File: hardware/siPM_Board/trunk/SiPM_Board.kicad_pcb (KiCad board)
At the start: 2 copper layers, 25 parts, among them J1 Conn_02x34_Odd_Even, J2 Conn_02x34_Odd_Even, U1 LM94021, U2 S14161-6050HS-04, U3 S14161-6050HS-04, U4 S14161-6050HS-04, U5 S14161-6050HS-04

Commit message: Layout Needs Editing
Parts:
- C1, C10, C11, C12, C13, C14, C15, C16, C17, C18, C2, C3, C4, C5, C6, C7, C8, C9, J1, J2, U1: moved to B.Cu
- moved U5 60.6 mm to (156.0, 88.5)
- moved U2 60.0 mm to (130.5, 88.5)
- moved C17 44.6 mm to (138.1, 92.1), turned to 90 degrees
- moved C13 39.9 mm to (141.5, 92.1), turned to 90 degrees
- moved C16 36.3 mm to (138.1, 98.2), turned to 90 degrees
- moved J1 36.1 mm to (130.5, 101.5), turned to 270 degrees
- moved C9 35.3 mm to (144.8, 92.1), turned to 90 degrees
- moved U1 32.7 mm to (143.2, 117.7)
- moved C18 32.5 mm to (141.4, 83.5), turned to 90 degrees
- moved C12 31.7 mm to (141.5, 98.2), turned to 90 degrees
- moved C5 30.7 mm to (148.2, 92.1), turned to 90 degrees
- moved C1 28.2 mm to (144.8, 83.5), turned to 90 degrees
- moved C15 28.0 mm to (138.1, 104.2), turned to 90 degrees
- moved C8 27.1 mm to (144.8, 98.2), turned to 90 degrees
- moved U3 26.8 mm to (130.5, 114.0)
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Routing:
- added copper zone on SiPM_Bias_voltage, net /BIAS1
- added copper zone on GND, net GND
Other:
- board outline added: 50.7 x 50.7 mm
- copper layers 2 -> 4

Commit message: Modified Perliminary Layout
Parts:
- moved U4 25.5 mm to (155.9, 88.5)
- moved U5 25.5 mm to (156.0, 114.0)
- turned J2 to 270 degrees

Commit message: Schematic changes made
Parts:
- removed C11, C12, C13, C14, C15, C16, C17, C18: 100nF, Capacitor_SMD:C_1206_3216Metric_Pad1.33x1.80mm_HandSolder
- C1, C10, C2, C3, C4, C5, C6, C7, C8, C9: footprint Capacitor_SMD:C_1206_3216Metric_Pad1.33x1.80mm_HandSolder -> Capacitor_SMD:C_0603_1608Metric_Pad1.08x0.95mm_HandSolder
- U1: footprint TO_SOT_Packages_SMD:Texas_R-PDSO-G6 -> Arich_SiPM_Footprints:Texas_R-PDSO-G6
- moved C1 16.5 mm to (139.4, 99.2), turned to 270 degrees
- moved C9 14.8 mm to (141.1, 106.5), turned to 180 degrees
- moved C2 12.7 mm to (141.9, 99.2), turned to 270 degrees
- moved C6 11.3 mm to (147.3, 99.2), turned to 270 degrees
- moved C4 9.50 mm to (140.3, 103.4), turned to 270 degrees
- moved C5 7.98 mm to (144.4, 99.2), turned to 270 degrees
- moved C3 6.21 mm to (142.0, 103.4), turned to 270 degrees
- moved C10 5.40 mm to (145.3, 106.4), turned to 180 degrees
- moved C8 5.39 mm to (144.4, 103.5), turned to 270 degrees
- moved C7 2.21 mm to (146.9, 103.4), turned to 270 degrees
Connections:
- C10 pad 1: /BIAS2 -> /OUT
- C3 pad 1: /BIAS1 -> /BIAS2
- C4 pad 1: /BIAS1 -> /BIAS2
- C5 pad 1: /BIAS1 -> /BIAS3
- C6 pad 1: /BIAS1 -> /BIAS3
- C7 pad 1: /BIAS1 -> /BIAS4
- C7 pad 2: GND -> Net-(C7-Pad2)
- C8 pad 1: /BIAS1 -> /BIAS4
- C8 pad 2: GND -> Net-(C7-Pad2)
- C9 pad 1: /BIAS2 -> /VDD
- J1 pad 2: GND -> /BIAS1
- J1 pad 66: /OUT -> GND
- J1 pad 67: /BIAS1 -> /BIAS2
- J1 pad 68: /BIAS1 -> /OUT
- J2 pad 2: GND -> /BIAS3
- J2 pad 66: Net-(J2-Pad66) -> GND
- J2 pad 67: /BIAS2 -> /BIAS4
- J2 pad 68: /BIAS2 -> /BIAS4
- U3 pad B1: /BIAS1 -> /BIAS2
- U3 pad B3: /BIAS1 -> /BIAS2
- U3 pad B5: /BIAS1 -> /BIAS2
- U3 pad B7: /BIAS1 -> /BIAS2
- U3 pad D1: /BIAS1 -> /BIAS2
- U3 pad D3: /BIAS1 -> /BIAS2
- U3 pad D5: /BIAS1 -> /BIAS2
- U3 pad D7: /BIAS1 -> /BIAS2
- U3 pad F2: /BIAS1 -> /BIAS2
- U3 pad F4: /BIAS1 -> /BIAS2
- U3 pad F6: /BIAS1 -> /BIAS2
- U3 pad F8: /BIAS1 -> /BIAS2
- U3 pad H2: /BIAS1 -> /BIAS2
- U3 pad H4: /BIAS1 -> /BIAS2
- U3 pad H6: /BIAS1 -> /BIAS2
- U3 pad H8: /BIAS1 -> /BIAS2
- U4 pad B1: /BIAS2 -> /BIAS3
- U4 pad B3: /BIAS2 -> /BIAS3
- U4 pad B5: /BIAS2 -> /BIAS3
- U4 pad B7: /BIAS2 -> /BIAS3
- U4 pad D1: /BIAS2 -> /BIAS3
- U4 pad D3: /BIAS2 -> /BIAS3
- U4 pad D5: /BIAS2 -> /BIAS3
- U4 pad D7: /BIAS2 -> /BIAS3
- U4 pad F2: /BIAS2 -> /BIAS3
- U4 pad F4: /BIAS2 -> /BIAS3
- U4 pad F6: /BIAS2 -> /BIAS3
- U4 pad F8: /BIAS2 -> /BIAS3
- U4 pad H2: /BIAS2 -> /BIAS3
- U4 pad H4: /BIAS2 -> /BIAS3
- U4 pad H6: /BIAS2 -> /BIAS3
- U4 pad H8: /BIAS2 -> /BIAS3
- U5 pad B1: /BIAS2 -> /BIAS4
- U5 pad B3: /BIAS2 -> /BIAS4
- U5 pad B5: /BIAS2 -> /BIAS4
- U5 pad B7: /BIAS2 -> /BIAS4
- U5 pad D1: /BIAS2 -> /BIAS4
- U5 pad D3: /BIAS2 -> /BIAS4
- U5 pad D5: /BIAS2 -> /BIAS4
- U5 pad D7: /BIAS2 -> /BIAS4
- U5 pad F2: /BIAS2 -> /BIAS4
- U5 pad F4: /BIAS2 -> /BIAS4
- U5 pad F6: /BIAS2 -> /BIAS4
- U5 pad F8: /BIAS2 -> /BIAS4
- U5 pad H2: /BIAS2 -> /BIAS4
- U5 pad H4: /BIAS2 -> /BIAS4
- U5 pad H6: /BIAS2 -> /BIAS4
- U5 pad H8: /BIAS2 -> /BIAS4

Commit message: Tracing incomplete
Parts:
- moved U1 5.64 mm to (143.3, 112.0), turned to 180 degrees
- moved C10 2.56 mm to (143.2, 107.9), turned to 0 degrees
- moved C6 2.16 mm to (145.4, 100.1), turned to 180 degrees
- moved C9 2.11 mm to (143.2, 106.2), turned to 0 degrees
- moved C1 2.04 mm to (141.2, 100.1), turned to 0 degrees
- moved C7 1.74 mm to (145.4, 104.3), turned to 180 degrees
- moved C8 1.47 mm to (145.4, 102.5), turned to 180 degrees
- moved C5 1.36 mm to (145.4, 98.2), turned to 180 degrees
- moved C3 1.28 mm to (141.2, 102.5), turned to 0 degrees
- moved C4 1.21 mm to (141.2, 104.2), turned to 0 degrees
- moved C2 1.14 mm to (141.2, 98.3), turned to 0 degrees
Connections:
- C7 pad 2: Net-(C7-Pad2) -> GND
- C8 pad 2: Net-(C7-Pad2) -> GND
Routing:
- net GND: track 0.00 -> 87.1 mm, vias 0 -> 17
- net /BIAS2: track 0.00 -> 5.15 mm, vias 0 -> 2
- net /BIAS1: track 0.00 -> 4.95 mm, vias 0 -> 2
- net /BIAS3: track 0.00 -> 3.40 mm, vias 0 -> 1
- net /BIAS4: track 0.00 -> 3.40 mm, vias 0 -> 1
- net Net-(J1-Pad1): track 0.00 -> 2.46 mm, vias 0 -> 1
- net Net-(J1-Pad45): track 0.00 -> 1.79 mm, vias 0 -> 1
- net /VDD: track 0.00 -> 1.78 mm, vias 0 -> 1
- net Net-(J1-Pad59): track 0.00 -> 1.78 mm, vias 0 -> 1
- net Net-(J1-Pad57): track 0.00 -> 1.78 mm, vias 0 -> 1
- net Net-(J1-Pad55): track 0.00 -> 1.78 mm, vias 0 -> 1
- net Net-(J1-Pad53): track 0.00 -> 1.78 mm, vias 0 -> 1
- net Net-(J1-Pad39): track 0.00 -> 1.78 mm, vias 0 -> 1
- net Net-(J1-Pad15): track 0.00 -> 1.78 mm, vias 0 -> 1
- net Net-(J1-Pad7): track 0.00 -> 1.78 mm, vias 0 -> 1
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- added copper zone on SiPM_Bias_voltage, net /BIAS2
- added copper zone on SiPM_Bias_voltage, net /BIAS3
- added copper zone on SiPM_Bias_voltage, net /BIAS4

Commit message: Tracing incomplete
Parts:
- moved C9 8.91 mm to (152.0, 104.6)
- moved C10 8.87 mm to (152.0, 106.3)
- moved U1 8.21 mm to (148.2, 105.5), turned to 90 degrees
- moved J1 7.03 mm to (137.4, 100.0)
- moved C4 6.99 mm to (148.0, 102.8)
- moved C3 6.98 mm to (148.0, 101.1)
- moved C1 6.93 mm to (148.0, 98.9)
- moved C2 6.92 mm to (148.0, 97.2)
- moved U4 6.91 mm to (162.8, 87.2)
- moved U3 6.86 mm to (137.2, 112.8)
- moved U5 6.86 mm to (162.8, 112.8)
- moved U2 6.85 mm to (137.2, 87.2)
- moved J2 6.80 mm to (162.6, 100.0)
- moved C7 6.76 mm to (152.0, 102.8)
- moved C8 6.75 mm to (152.0, 101.1)
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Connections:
- J1 pad 67: /BIAS2 -> /OUT
- J1 pad 68: /OUT -> /BIAS2
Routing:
- net /BIAS1: track 4.95 -> 99.2 mm
- net GND: track 87.1 -> 149.2 mm, vias 17 -> 18
- net /VDD: track 1.78 -> 19.5 mm, vias 1 -> 0
- net /OUT: track 1.77 -> 18.9 mm, vias 1 -> 0
- net Net-(J1-Pad7): track 1.78 -> 15.9 mm
- net Net-(J1-Pad15): track 1.78 -> 14.8 mm
- net Net-(J1-Pad5): track 1.78 -> 13.9 mm
- net Net-(J1-Pad23): track 1.75 -> 12.7 mm
- net Net-(J1-Pad1): track 2.46 -> 12.5 mm
- net Net-(J1-Pad31): track 1.74 -> 11.1 mm
- net Net-(J1-Pad9): track 1.77 -> 10.6 mm
- net Net-(J1-Pad25): track 1.77 -> 10.5 mm
- net Net-(J1-Pad13): track 1.77 -> 9.54 mm
- net Net-(J1-Pad17): track 1.77 -> 9.12 mm
- net Net-(J1-Pad21): track 1.76 -> 7.20 mm
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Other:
- board size 50.7 x 50.7 mm -> 50.6 x 50.6 mm

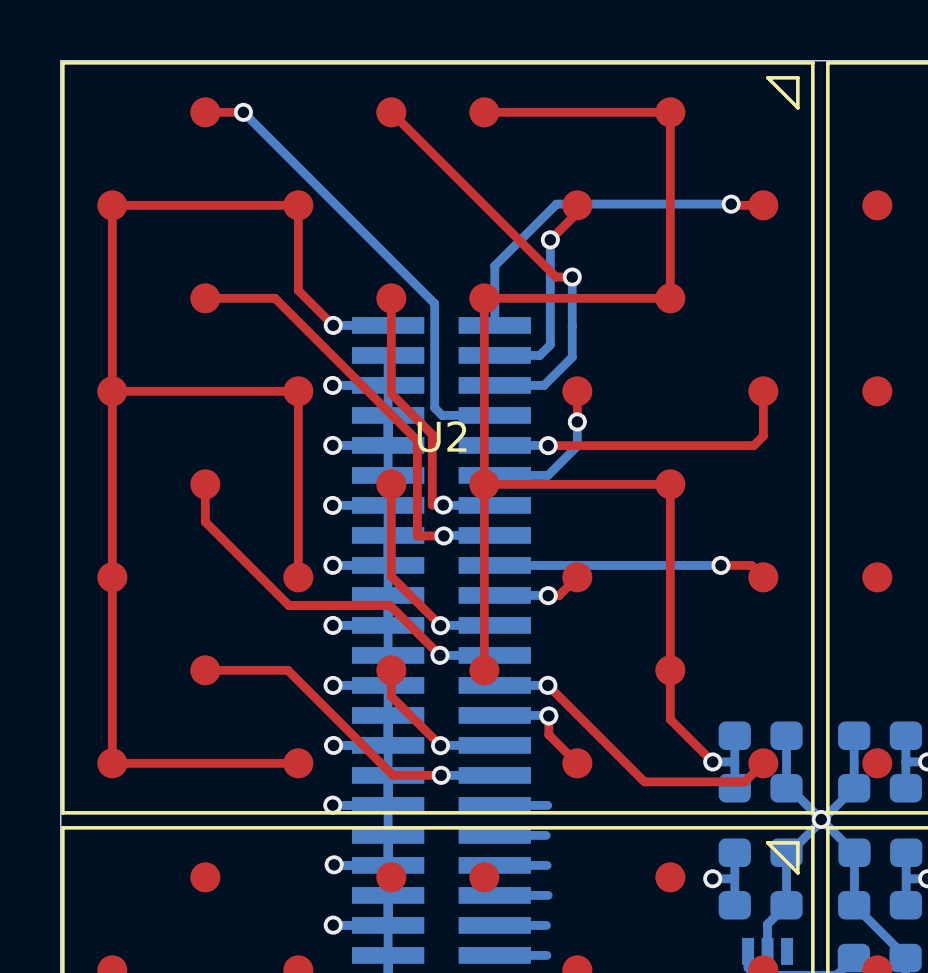
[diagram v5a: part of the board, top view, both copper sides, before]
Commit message: Routing of BIAS1 example
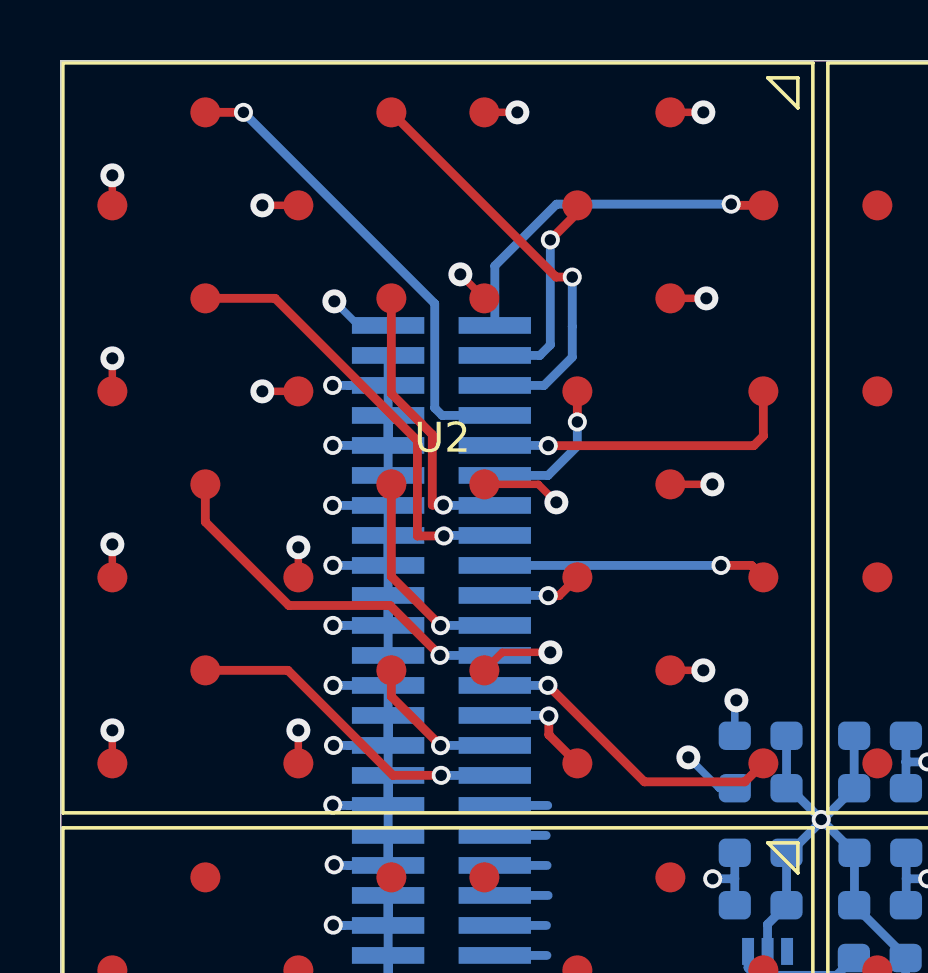
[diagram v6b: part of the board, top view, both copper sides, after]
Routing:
- net /BIAS1: track 99.2 -> 26.2 mm, vias 2 -> 19
